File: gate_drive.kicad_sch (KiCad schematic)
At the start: 111 parts, among them U1 EG2131, U10 EG2131, U12 EG2131, U2 EG2131, U3 LM358, U4 EG2131, U5 EG2131, U8 LM358

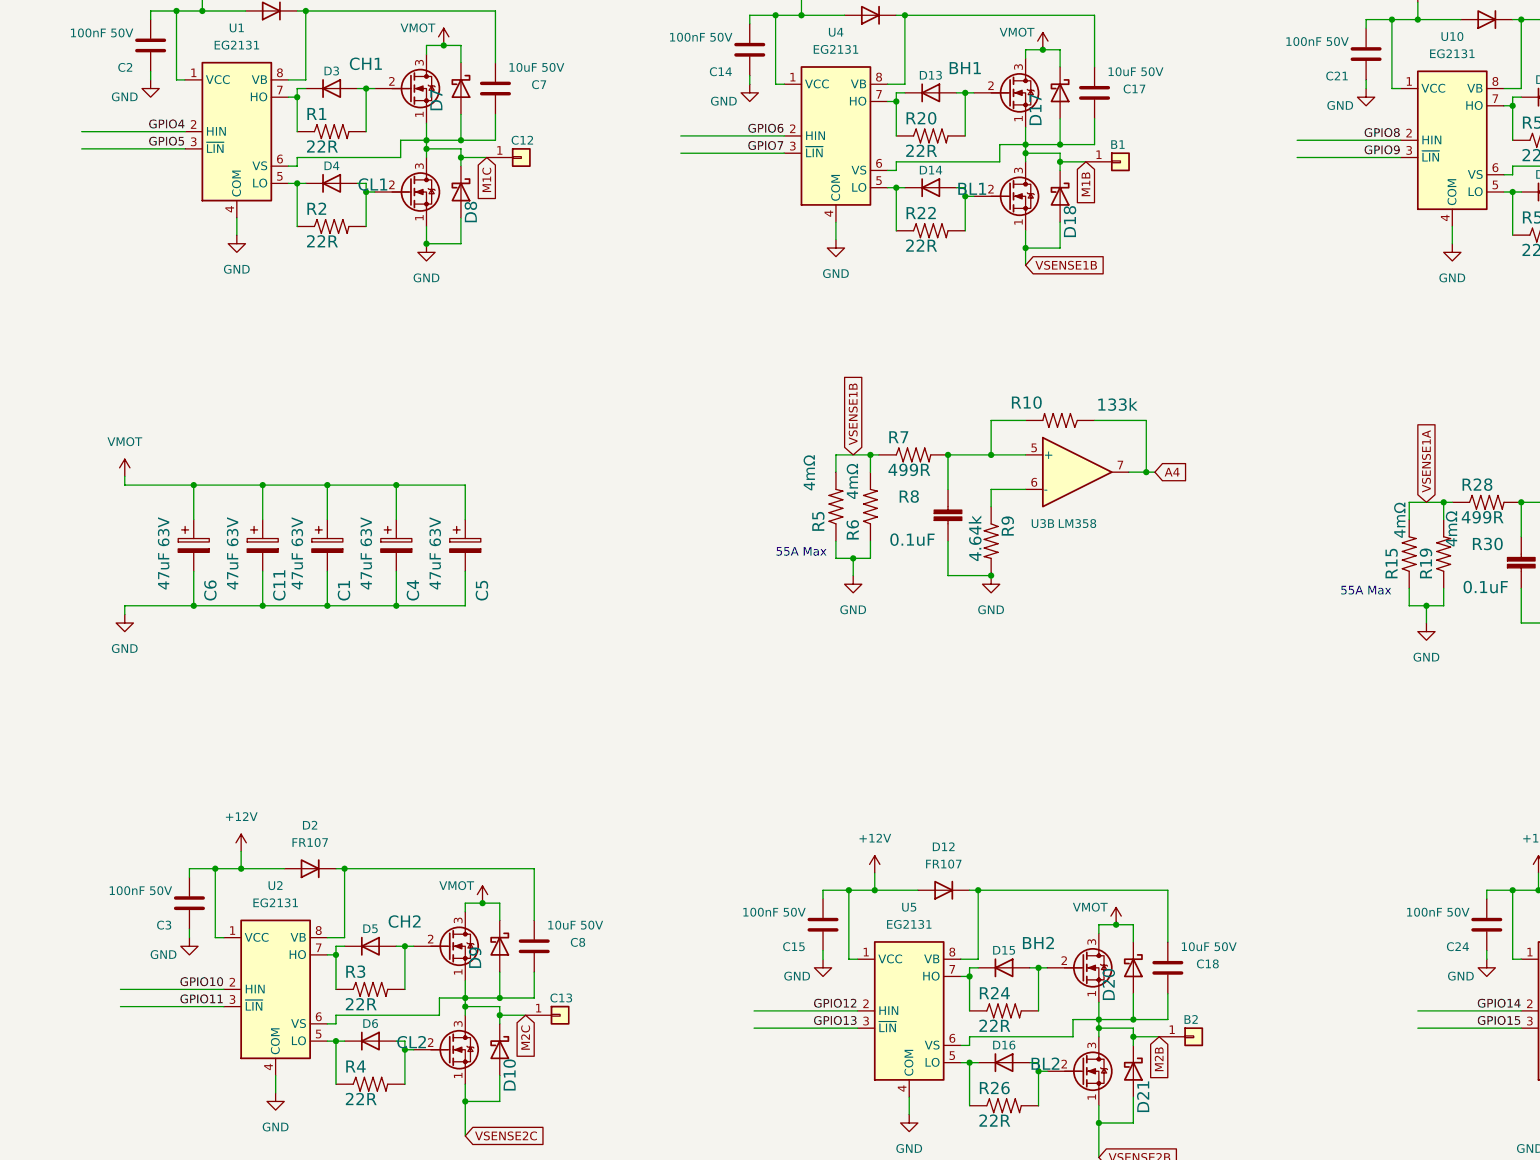
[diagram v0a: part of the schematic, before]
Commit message: Updated design rules and fixed routing to eliminate all copper DRC errors.
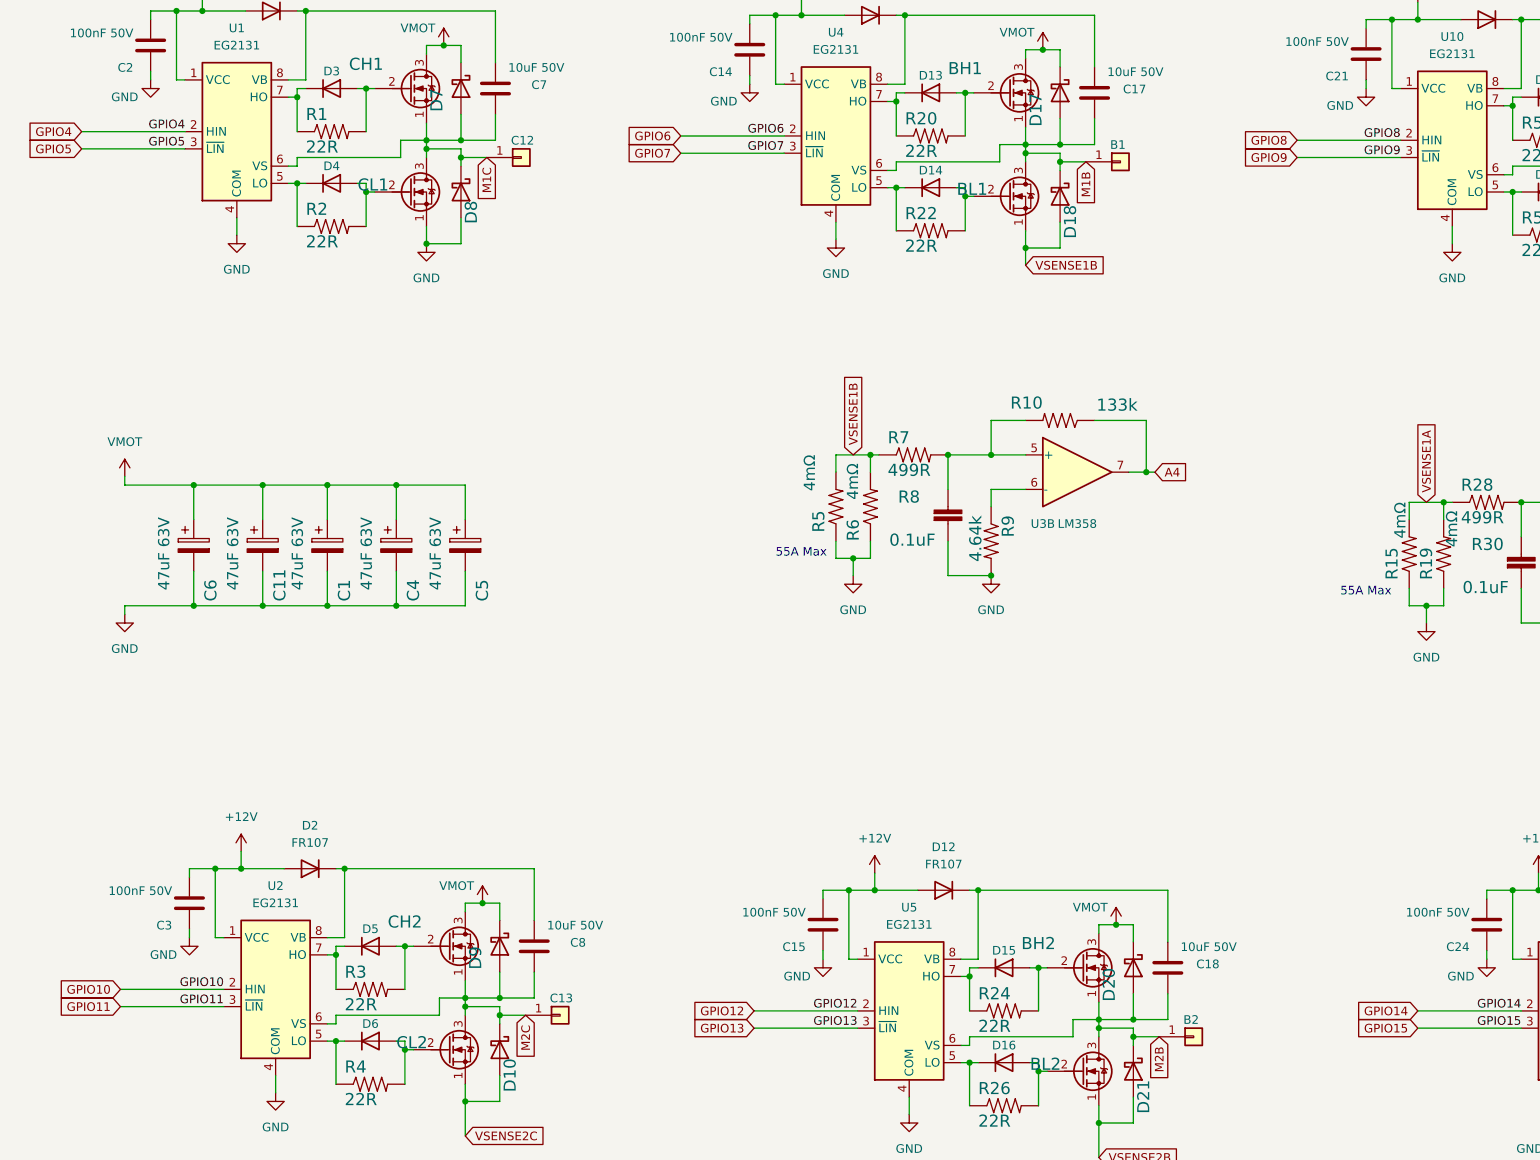
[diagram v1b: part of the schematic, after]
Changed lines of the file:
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@@
     (effects (font (size 1.27 1.27)) (justify right bottom))
+  )
+  (global_label "GPIO13" (shape input) (at 157.48 184.785 180) (fields_autoplaced)
+    (effects (font (size 1.27 1.27)) (justify right))
+    (property "Intersheet References" "${INTERSHEET_REFS}" (id 0) (at 148.2615 184.7056 0)
+      (effects (font (size 1.27 1.27)) (justify right) hide)
+    )
+  )
+  (global_label "GPIO15" (shape input) (at 255.27 184.785 180) (fields_autoplaced)
+    (effects (font (size 1.27 1.27)) (justify right))
+    (property "Intersheet References" "${INTERSHEET_REFS}" (id 0) (at 246.0515 184.7056 0)
+      (effects (font (size 1.27 1.27)) (justify right) hide)
+    )
   )
   (global_label "VSENSE2C" (shape input) (at 114.935 200.66 0) (fields_autoplaced)
@@
     (property "Intersheet References" "${INTERSHEET_REFS}" (id 0) (at 126.8749 200.5806 0)
       (effects (font (size 1.27 1.27)) (justify left) hide)
+    )
+  )
+  (global_label "GPIO7" (shape input) (at 146.685 55.88 180) (fields_autoplaced)
+    (effects (font (size 1.27 1.27)) (justify right))
+    (property "Intersheet References" "${INTERSHEET_REFS}" (id 0) (at 138.676 55.8006 0)
+      (effects (font (size 1.27 1.27)) (justify right) hide)
     )
   )
@@
     (effects (font (size 1.27 1.27)) (justify right))
     (property "Intersheet References" "${INTERSHEET_REFS}" (id 0) (at 314.8806 192.1287 90)
+      (effects (font (size 1.27 1.27)) (justify right) hide)
+    )
+  )
+  (global_label "GPIO10" (shape input) (at 64.135 179.07 180) (fields_autoplaced)
+    (effects (font (size 1.27 1.27)) (justify right))
+    (property "Intersheet References" "${INTERSHEET_REFS}" (id 0) (at 54.9165 178.9906 0)
+      (effects (font (size 1.27 1.27)) (justify right) hide)
+    )
+  )
+  (global_label "GPIO11" (shape input) (at 64.135 181.61 180) (fields_autoplaced)
+    (effects (font (size 1.27 1.27)) (justify right))
+    (property "Intersheet References" "${INTERSHEET_REFS}" (id 0) (at 54.9165 181.5306 0)
+      (effects (font (size 1.27 1.27)) (justify right) hide)
+    )
+  )
+  (global_label "GPIO14" (shape input) (at 255.27 182.245 180) (fields_autoplaced)
+    (effects (font (size 1.27 1.27)) (justify right))
+    (property "Intersheet References" "${INTERSHEET_REFS}" (id 0) (at 246.0515 182.1656 0)
       (effects (font (size 1.27 1.27)) (justify right) hide)
     )
@@
     )
   )
+  (global_label "GPIO4" (shape input) (at 58.42 52.705 180) (fields_autoplaced)
+    (effects (font (size 1.27 1.27)) (justify right))
+    (property "Intersheet References" "${INTERSHEET_REFS}" (id 0) (at 50.411 52.6256 0)
+      (effects (font (size 1.27 1.27)) (justify right) hide)
+    )
+  )
   (global_label "VSENSE2C" (shape input) (at 80.01 229.87 90) (fields_autoplaced)
     (effects (font (size 1.27 1.27)) (justify left))
     (property "Intersheet References" "${INTERSHEET_REFS}" (id 0) (at 79.9306 217.9301 90)
       (effects (font (size 1.27 1.27)) (justify left) hide)
+    )
+  )
+  (global_label "GPIO5" (shape input) (at 58.42 55.245 180) (fields_autoplaced)
+    (effects (font (size 1.27 1.27)) (justify right))
+    (property "Intersheet References" "${INTERSHEET_REFS}" (id 0) (at 50.411 55.1656 0)
+      (effects (font (size 1.27 1.27)) (justify right) hide)
     )
   )
@@
     )
   )
+  (global_label "GPIO9" (shape input) (at 237.49 56.515 180) (fields_autoplaced)
+    (effects (font (size 1.27 1.27)) (justify right))
+    (property "Intersheet References" "${INTERSHEET_REFS}" (id 0) (at 229.481 56.4356 0)
+      (effects (font (size 1.27 1.27)) (justify right) hide)
+    )
+  )
   (global_label "M1C" (shape input) (at 118.11 56.515 270) (fields_autoplaced)
     (effects (font (size 1.27 1.27)) (justify right))
@@
     )
   )
+  (global_label "GPIO6" (shape input) (at 146.685 53.34 180) (fields_autoplaced)
+    (effects (font (size 1.27 1.27)) (justify right))
+    (property "Intersheet References" "${INTERSHEET_REFS}" (id 0) (at 138.676 53.2606 0)
+      (effects (font (size 1.27 1.27)) (justify right) hide)
+    )
+  )
   (global_label "A3" (shape input) (at 300.99 109.855 0) (fields_autoplaced)
     (effects (font (size 1.27 1.27)) (justify left))
     (property "Intersheet References" "${INTERSHEET_REFS}" (id 0) (at 305.6123 109.7756 0)
       (effects (font (size 1.27 1.27)) (justify left) hide)
+    )
+  )
+  (global_label "GPIO8" (shape input) (at 237.49 53.975 180) (fields_autoplaced)
+    (effects (font (size 1.27 1.27)) (justify right))
+    (property "Intersheet References" "${INTERSHEET_REFS}" (id 0) (at 229.481 53.8956 0)
+      (effects (font (size 1.27 1.27)) (justify right) hide)
     )
   )
@@
     )
   )
+  (global_label "GPIO12" (shape input) (at 157.48 182.245 180) (fields_autoplaced)
+    (effects (font (size 1.27 1.27)) (justify right))
+    (property "Intersheet References" "${INTERSHEET_REFS}" (id 0) (at 148.2615 182.1656 0)
+      (effects (font (size 1.27 1.27)) (justify right) hide)
+    )
+  )

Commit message: I think layout is complete and the board is ready to order.
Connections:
- net VSENSE1A: now also R7.1; no longer R28.1
- net VSENSE1B: now also R28.1; no longer R7.1
- net VSENSE2B: now also R37.1; no longer R13.1
- net VSENSE2C: now also R13.1; no longer R37.1
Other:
- moved on the sheet: R10, R11, R12, R13, R14, R15, R18, R19, R28, R29, R30, R31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
